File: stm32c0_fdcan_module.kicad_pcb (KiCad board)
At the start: 2 copper layers, 28 x 26.5 mm, 32 parts, among them IC1 STM32C092GCU6, IC2 TJA1051TK_3,118, J1 12505WS-04, J2 Conn_01x10, J3 Conn_01x10, J4 12505WS-06, SW1 DSHP02TSGER, U1 XC6206P332MR, Y1 8MHz_50X32mm

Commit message: 단면 배치 버전
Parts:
- C1, C2, C5, C6, C7, C8, C9, D1, D2, R1, R2, R3, R4, R7: moved to F.Cu
- moved R2 39.6 mm to (140.5, 82.0), turned to 90 degrees
- moved 3.3V1 39.5 mm to (140.5, 85.0), turned to -90 degrees
- moved R3 35.3 mm to (142.0, 82.0), turned to 90 degrees
- moved CPU1 35.3 mm to (142.0, 85.0), turned to -90 degrees
- moved C2 32.8 mm to (133.5, 84.5)
- moved U1 32.6 mm to (133.4, 81.1)
- moved C10 30.5 mm to (131.5, 99.5)
- moved C1 30.1 mm to (130.0, 81.0), turned to -90 degrees
- moved J4 29.0 mm to (137.0, 72.1)
- moved C9 27.6 mm to (127.5, 75.0), turned to 0 degrees
- moved D2 27.3 mm to (123.0, 71.5)
- moved C11 26.3 mm to (126.5, 92.0)
- moved J3 25.7 mm to (145.0, 87.5)
- moved Y1 25.4 mm to (126.5, 97.0), turned to 90 degrees
- moved J1 24.8 mm to (113.9, 74.2), turned to 180 degrees
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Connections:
- J2 pad 1: 5V -> +3.3V
- J2 pad 2: 5V -> GND
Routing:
- net +3.3V: track 33.4 -> 76.7 mm, vias 7 -> 4
- net SWCLK: track 7.41 -> 47.7 mm
- net SWDIO: track 6.43 -> 46.1 mm
- net UART1_TX: track 9.33 -> 38.2 mm
- net LED: track 2.17 -> 27.7 mm
- net UART1_RX: track 12.5 -> 37.4 mm
- net Net-(R1-Pad1): track 26.5 -> 3.02 mm, vias 1 -> 0
- net CAN_L: track 16.9 -> 40.2 mm
- net FDCAN_TX: track 12.2 -> 31.8 mm, vias 0 -> 2
- net FDCAN_RX: track 10.1 -> 27.6 mm, vias 0 -> 2
- net PB5: track 13.9 -> 22.8 mm
- net PB6: track 15.5 -> 23.7 mm
- net PB4: track 14.0 -> 22.0 mm
- net nRST: track 20.6 -> 12.7 mm
- net PA12: track 15.6 -> 23.4 mm
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- added copper zone on F.Cu, net +3.3V
- added copper zone on F.Cu, net Net-(D2-A)
- removed copper zone on B.Cu, net 5V
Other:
- board size 28 x 26.5 mm -> 45 x 42 mm
- board text added: "3.3V"
- board text added: "Botton"
- board text added: "GLH5"
- board text added: "GND"
- board text added: "LED"
- board text added: "PA11"
- board text added: "PA12"
- board text added: "PA15"
- board text added: "PA3"
- board text added: "PA4"
- board text added: "PA5"
- board text added: "PA6"
- board text added: "PA7"
- board text added: "PA8"
- board text added: "PB3"
- board text added: "PB4"
- board text added: "PB5"
- board text added: "PB6"
- board text added: "PC6"
- board text added: "RTGCD3"
- board text added: "Reset"
- board text added: "VCC"
- board text removed: "25.04.27"
- board text removed: "STM32C0 FDCAN Board"

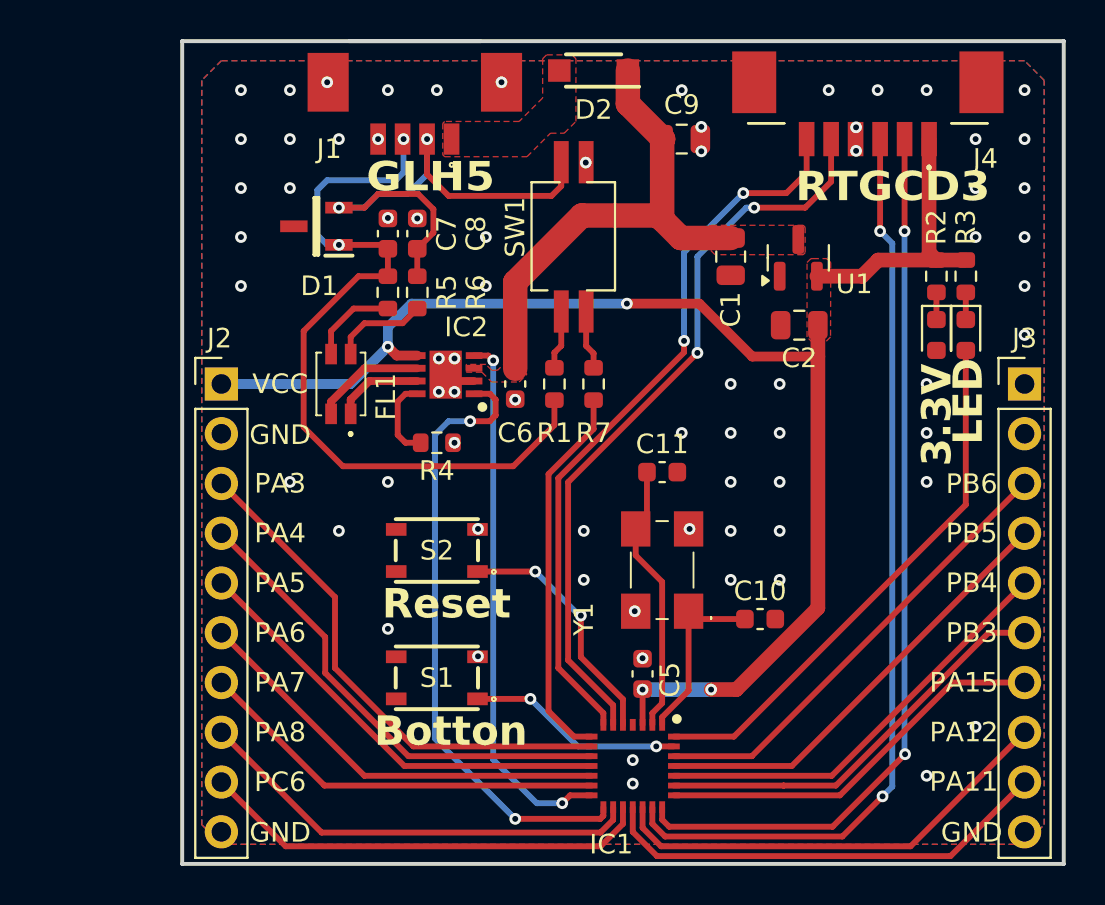
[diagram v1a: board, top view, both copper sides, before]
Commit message: PCB 라우팅 수정 - 하단부 이격
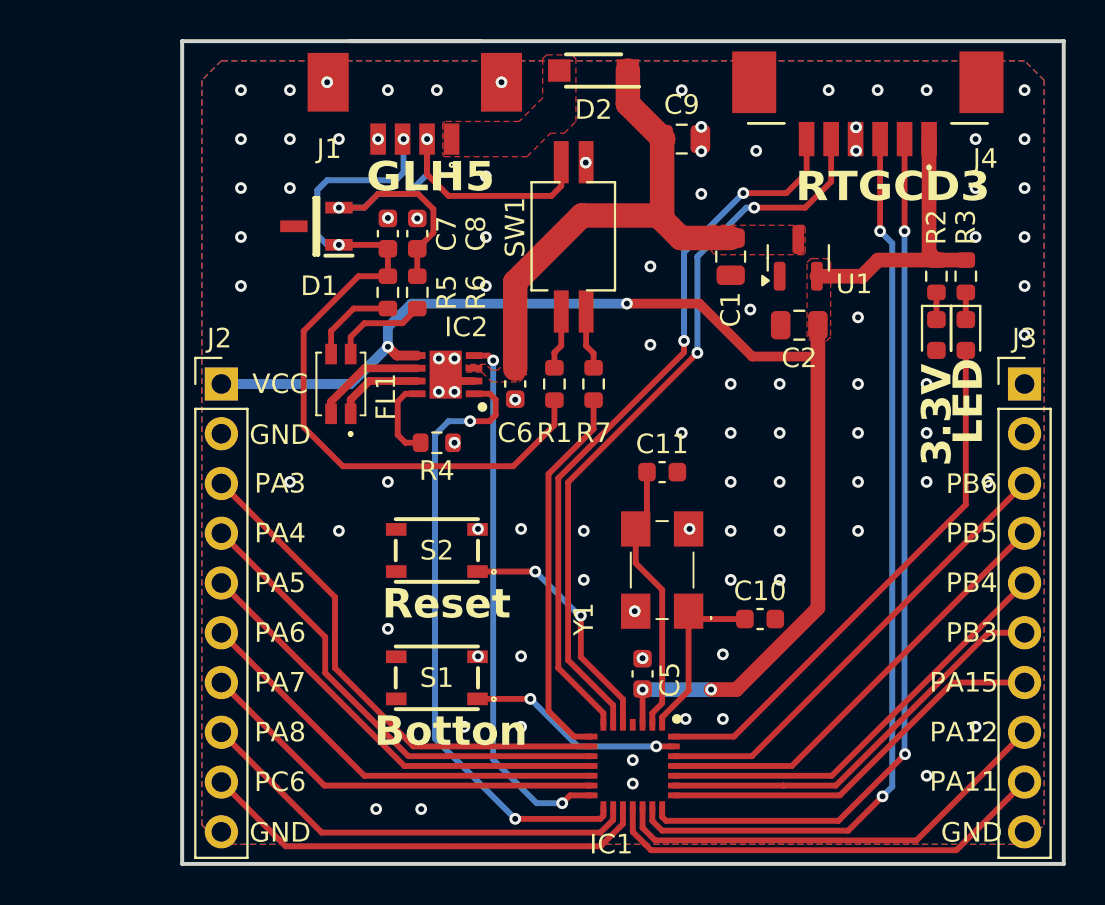
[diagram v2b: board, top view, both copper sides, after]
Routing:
- net GND: vias 71 -> 92

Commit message: BOM, SMT, 거버 추가 및 일부 라우팅 수정
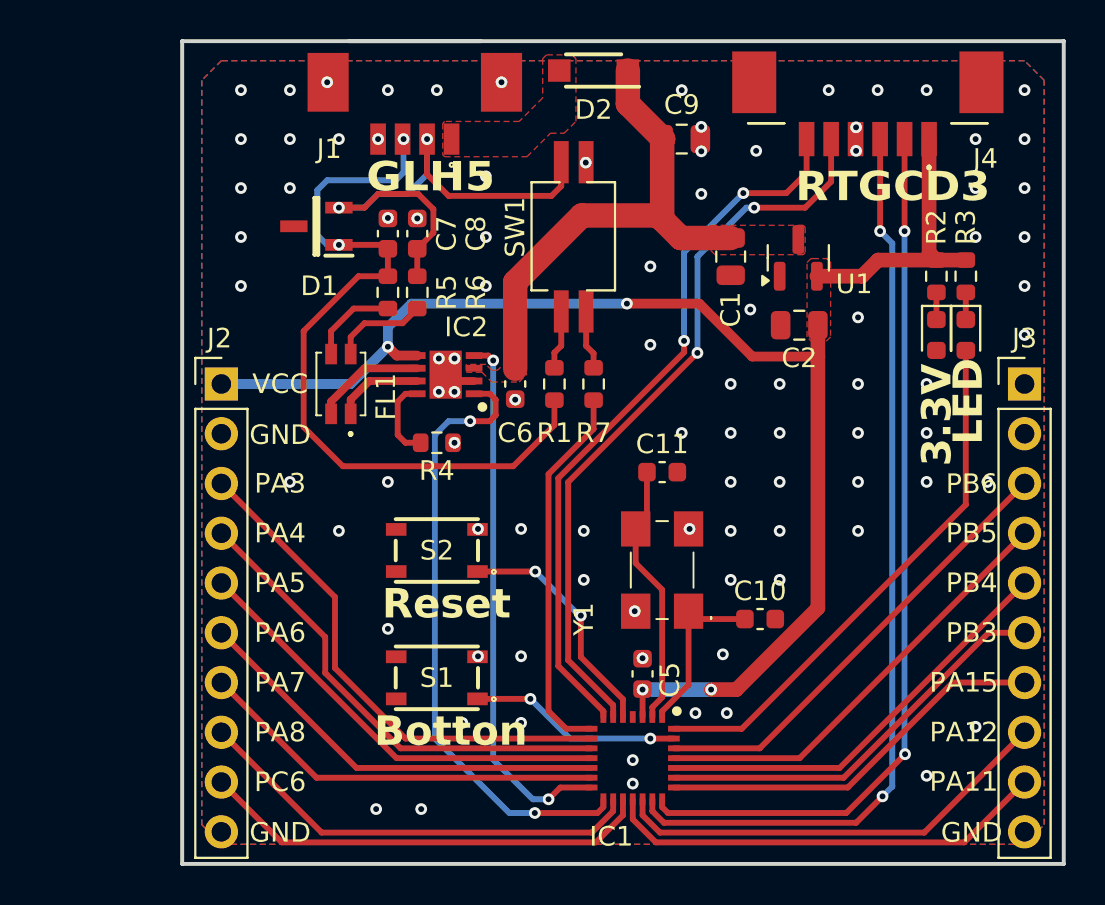
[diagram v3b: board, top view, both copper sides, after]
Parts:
- moved IC1 0.40 mm to (125.0, 106.6)
